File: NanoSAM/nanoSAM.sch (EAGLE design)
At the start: 76 parts, among them IC3 AD5241, J1 POWER_JACK, U1 LTC3260EMSEPBF

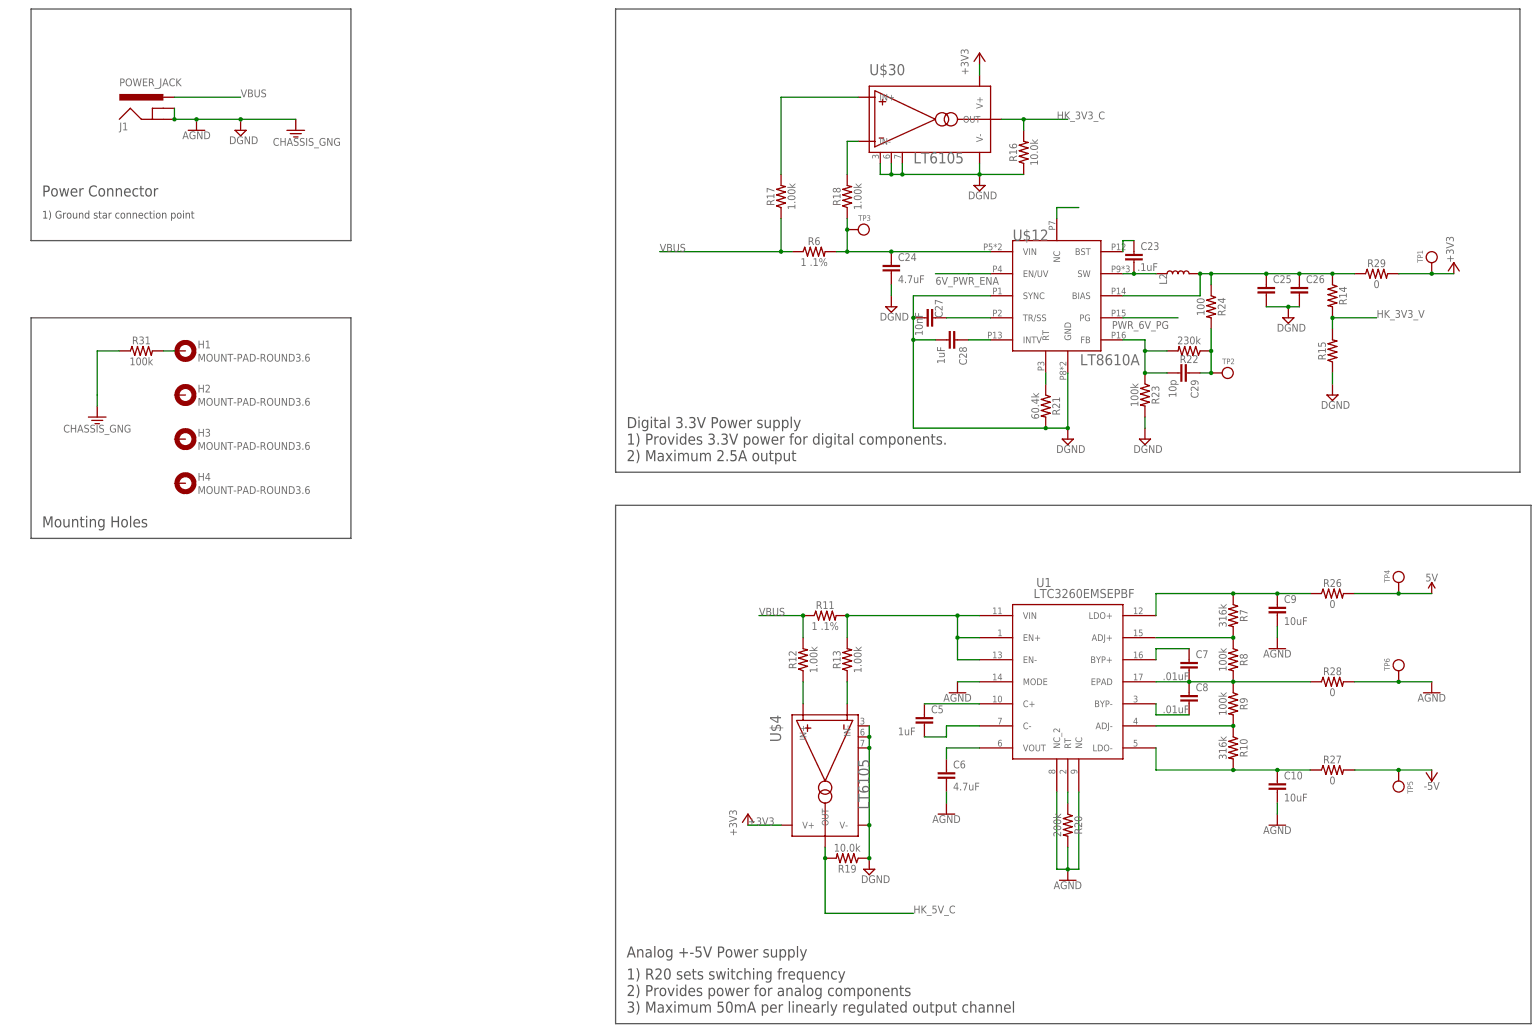
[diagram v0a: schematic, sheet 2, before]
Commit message: added thermistors for temp monitoring and changed current monitoring circuit
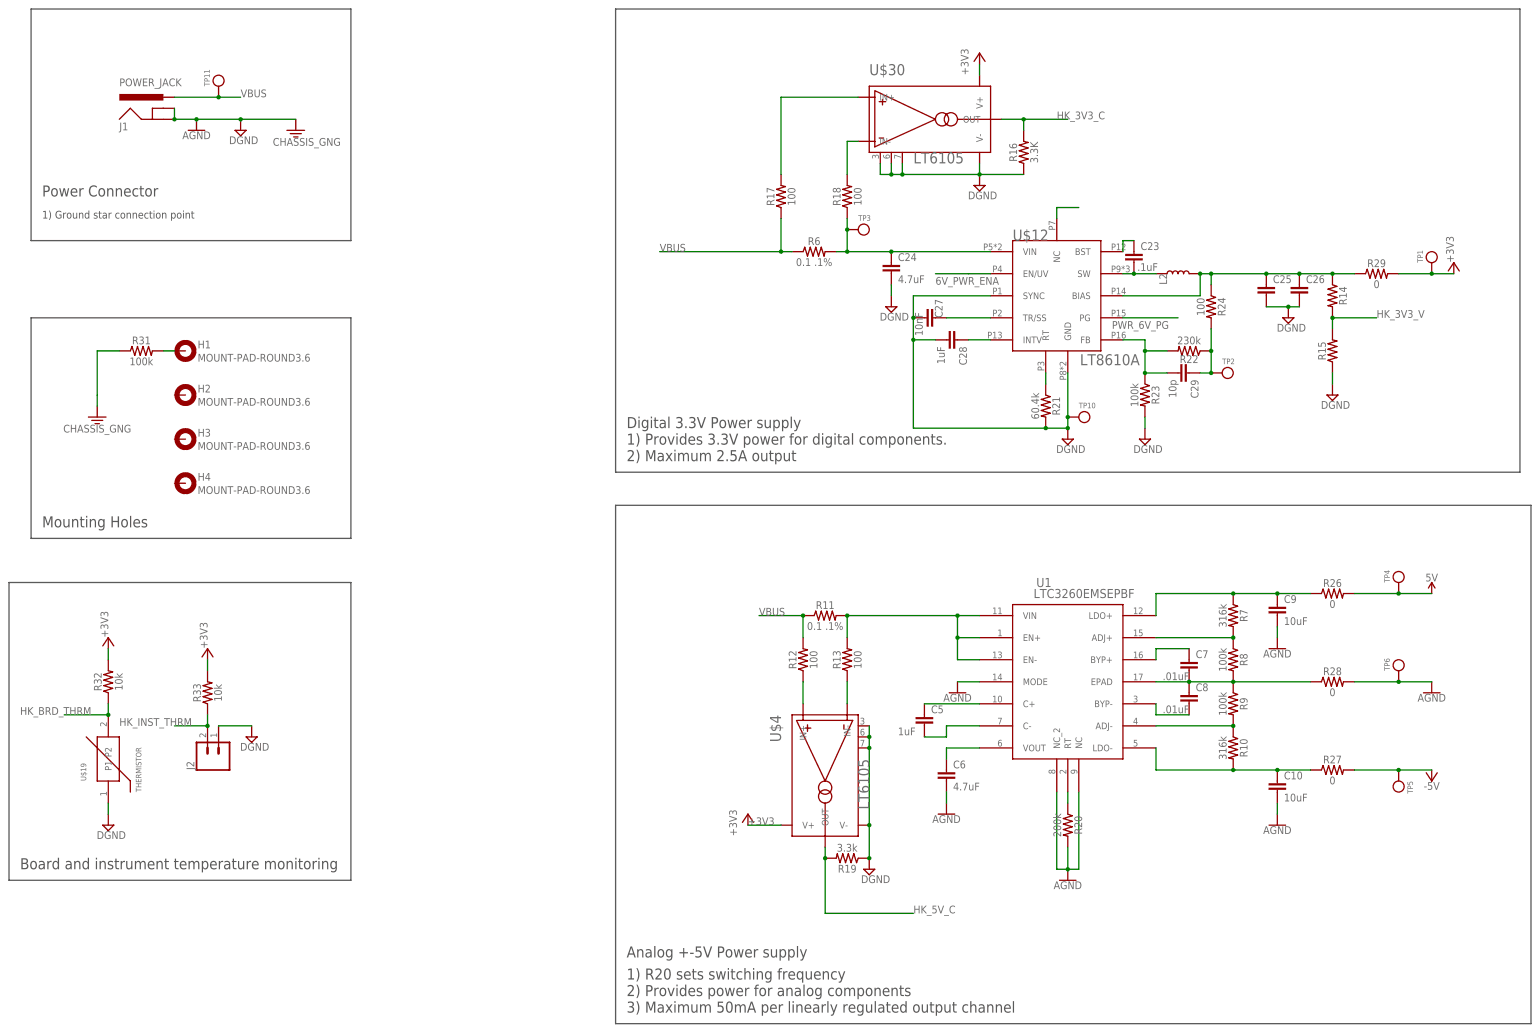
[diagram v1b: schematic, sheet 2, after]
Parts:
- added J2: (no value), SparkFun-Connectors:CONN_02
- added R32, R33: 10k, SparkFun-Resistors:RESISTOR1206
- added TP10, TP11, TP7, TP8, TP9: (no value), testpoint:TESTPOINT
- added U$19: THERMISTOR, 0805_Thermistor:THERMISTOR
- R11, R6: value 1 .1% -> 0.1 .1%
- R12, R13, R17, R18: value 1.00k -> 100
- R16: value 10.0k -> 3.3K
- R19: value 10.0k -> 3.3k
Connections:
- new net HK_BRD_THRM: R32.1, U$19.P2
- new net HK_INST_THRM: J2.2, R33.1
- net +3V3: now also R32.2, R33.2
- net AGND: now also TP9.P$1
- net DGND: now also J2.1, TP10.P$1, U$19.P1
- net N$1: now also TP8.P$1
- net N$3: now also TP7.P$1
- net VBUS: now also TP11.P$1
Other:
- note added: "Board and instrument temperature monitoring"

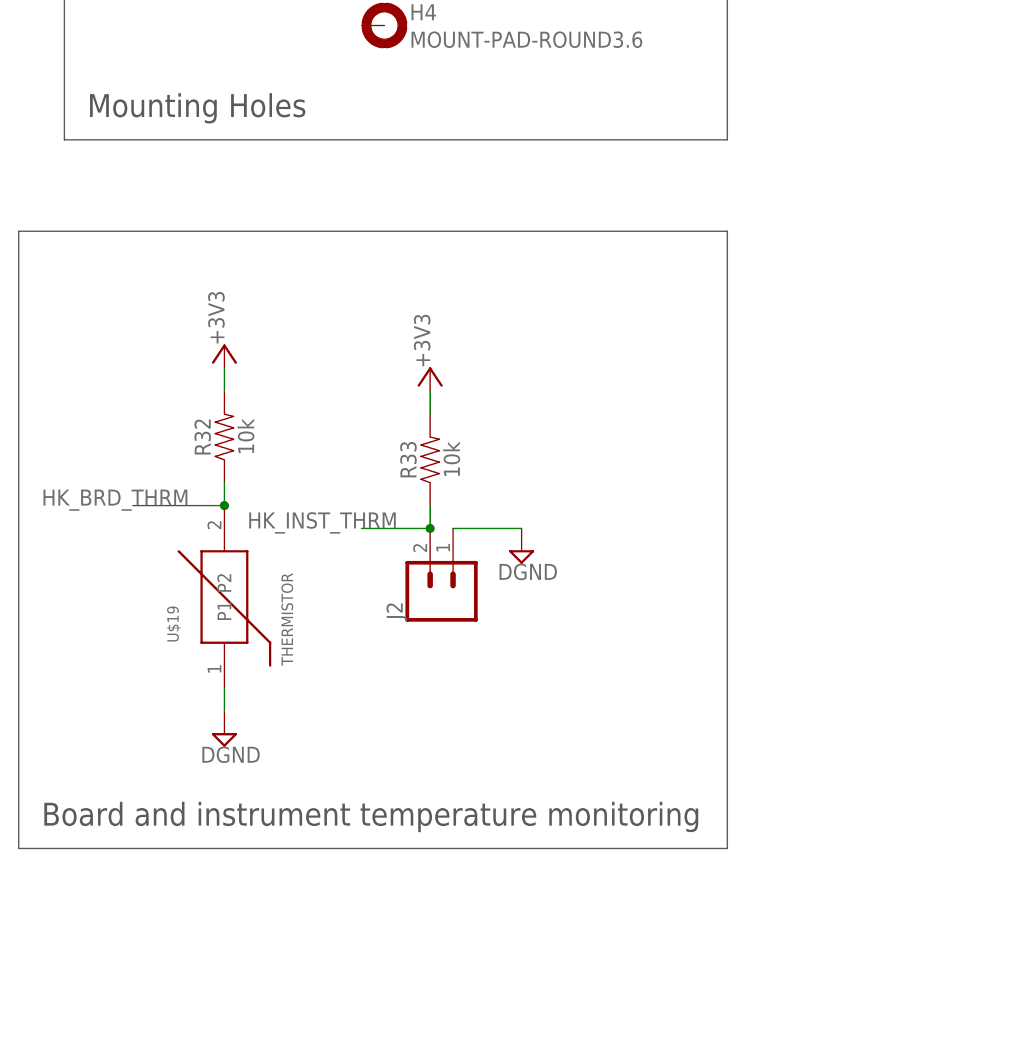
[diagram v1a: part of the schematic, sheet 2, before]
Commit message: added more thermistor connections
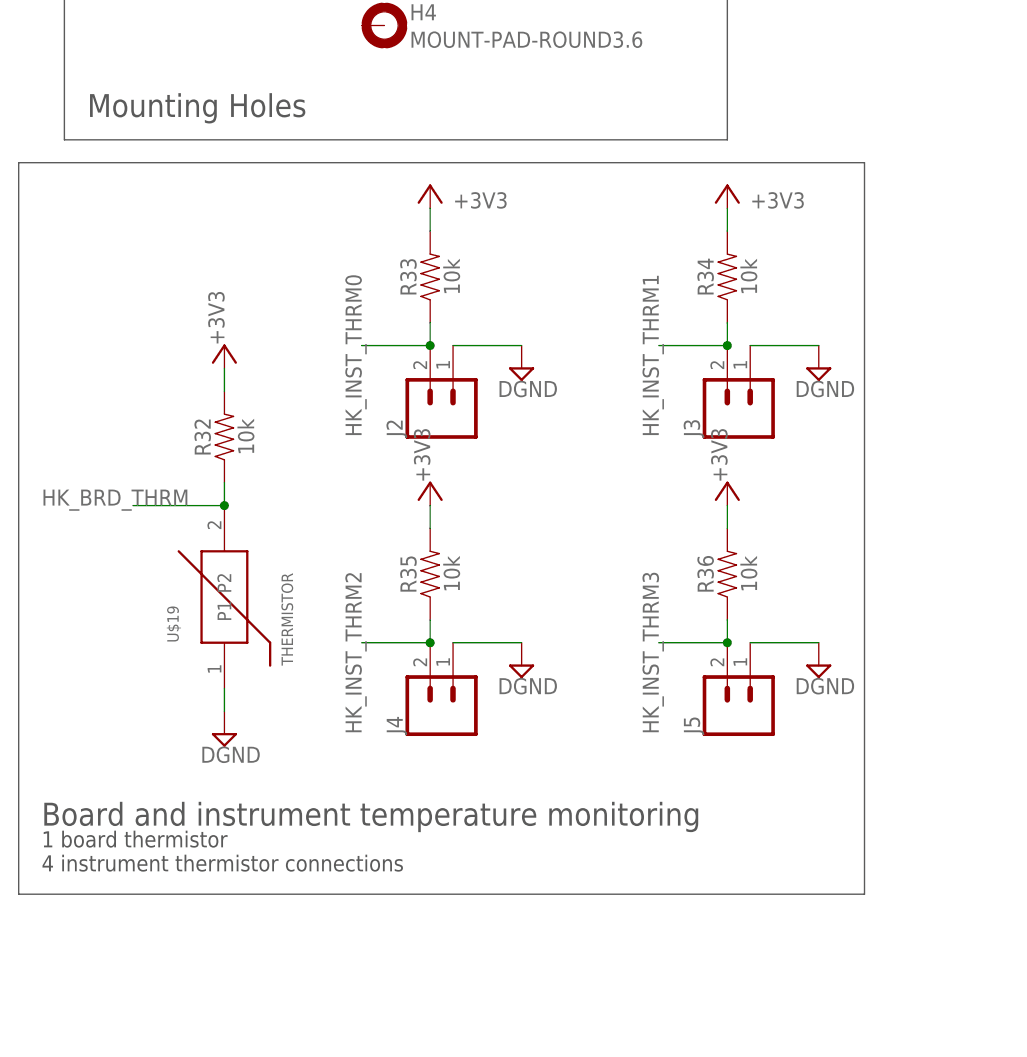
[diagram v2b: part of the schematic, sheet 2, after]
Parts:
- added J3, J4, J5: (no value), SparkFun-Connectors:CONN_02
- added R34, R35, R36: 10k, SparkFun-Resistors:RESISTOR1206
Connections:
- removed net HK_INST_THRM: J2.2, R33.1
- removed net HK_THRM: U$2.D17/A3
- removed net N$25: C4.2, IC3.NC, IC3.VSS
- new net HK_INST_THRM0: J2.2, R33.1, U$2.D20/A6
- new net HK_INST_THRM1: J3.2, R34.1, U$2.D21/A7
- new net HK_INST_THRM2: J4.2, R35.1, U$2.D22/A8
- new net HK_INST_THRM3: J5.2, R36.1, U$2.D23/A9
- net +3V3: now also R34.2, R35.2, R36.2
- net DGND: now also C4.2, IC3.NC, IC3.VSS, J3.1, J4.1, J5.1
- net HK_BRD_THRM: now also U$2.D17/A3
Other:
- note added: "1 board thermistor 4 instrument thermistor connections"
- moved on the sheet: J2, R33

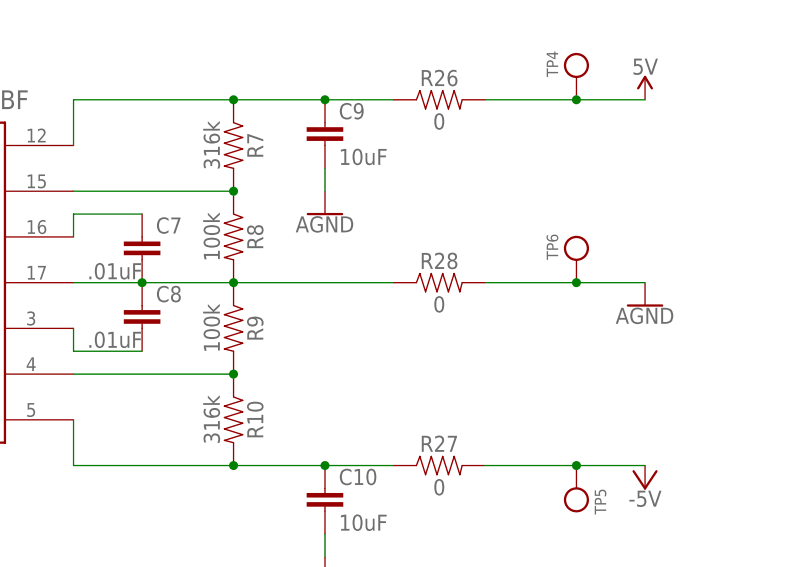
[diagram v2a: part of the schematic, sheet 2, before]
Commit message: Edited Bipolar power supply
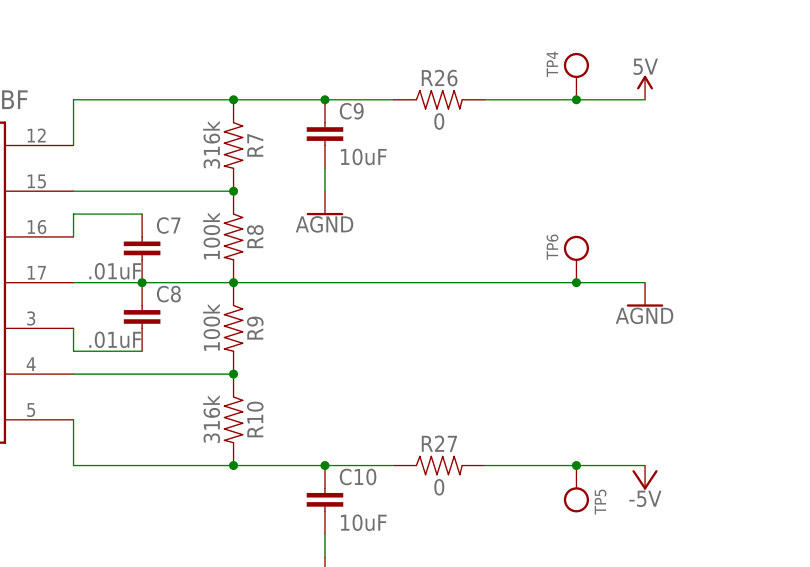
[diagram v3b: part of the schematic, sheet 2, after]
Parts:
- removed R28: 0, SparkFun-Resistors:RESISTOR0603
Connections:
- removed net N$26: C7.2, C8.1, R28.1, R8.2, R9.1, U1.EPAD
- net AGND: now also C7.2, C8.1, R8.2, R9.1, U1.EPAD; no longer R28.2
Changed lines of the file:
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@@
 <?xml version="1.0" encoding="utf-8"?>
 <!DOCTYPE eagle SYSTEM "eagle.dtd">
-<eagle version="9.3.0">
+<eagle version="9.5.1">
 <drawing>
 <settings>
@@
 <part name="R26" library="SparkFun-Resistors" library_urn="urn:adsk.eagle:library:532" deviceset="RESISTOR" device="0603" package3d_urn="urn:adsk.eagle:package:39650/1" value="0"/>
 <part name="R27" library="SparkFun-Resistors" library_urn="urn:adsk.eagle:library:532" deviceset="RESISTOR" device="0603" package3d_urn="urn:adsk.eagle:package:39650/1" value="0"/>
-<part name="R28" library="SparkFun-Resistors" library_urn="urn:adsk.eagle:library:532" deviceset="RESISTOR" device="0603" package3d_urn="urn:adsk.eagle:package:39650/1" value="0"/>
 <part name="TP1" library="testpoint" deviceset="TESTPOINT" device=""/>
 <part name="R29" library="SparkFun-Resistors" library_urn="urn:adsk.eagle:library:532" deviceset="RESISTOR" device="0603" package3d_urn="urn:adsk.eagle:package:39650/1" value="0"/>
@@
 <attribute name="VALUE" x="317.5" y="89.916" size="1.778" layer="96" font="vector" align="top-center"/>
 </instance>
-<instance part="R28" gate="G$1" x="317.5" y="111.76" smashed="yes">
-<attribute name="NAME" x="317.5" y="113.284" size="1.778" layer="95" font="vector" align="bottom-center"/>
-<attribute name="VALUE" x="317.5" y="110.236" size="1.778" layer="96" font="vector" align="top-center"/>
-</instance>
 <instance part="TP1" gate="G$1" x="340.36" y="208.28" smashed="yes" rot="R90">
 <attribute name="NAME" x="338.328" y="208.28" size="1.27" layer="95" rot="R90"/>
@@
 <pinref part="TP6" gate="G$1" pin="P$1"/>
 <junction x="332.74" y="111.76"/>
-<wire x1="322.58" y1="111.76" x2="332.74" y2="111.76" width="0.1524" layer="91"/>
-<pinref part="R28" gate="G$1" pin="2"/>
+<pinref part="R8" gate="G$1" pin="2"/>
+<pinref part="R9" gate="G$1" pin="1"/>
+<wire x1="294.64" y1="111.76" x2="284.48" y2="111.76" width="0.1524" layer="91"/>
+<junction x="294.64" y="111.76"/>
+<pinref part="U1" gate="A" pin="EPAD"/>
+<wire x1="284.48" y1="111.76" x2="276.86" y2="111.76" width="0.1524" layer="91"/>
+<pinref part="C7" gate="G$1" pin="2"/>
+<junction x="284.48" y="111.76"/>
+<pinref part="C8" gate="G$1" pin="1"/>
+<wire x1="294.64" y1="111.76" x2="332.74" y2="111.76" width="0.1524" layer="91"/>
 </segment>
 <segment>
@@
 </segment>
 </net>
-<net name="N$26" class="0">
-<segment>
-<pinref part="R8" gate="G$1" pin="2"/>
-<pinref part="R9" gate="G$1" pin="1"/>
-<wire x1="294.64" y1="111.76" x2="284.48" y2="111.76" width="0.1524" layer="91"/>
-<junction x="294.64" y="111.76"/>
-<pinref part="U1" gate="A" pin="EPAD"/>
-<wire x1="284.48" y1="111.76" x2="276.86" y2="111.76" width="0.1524" layer="91"/>
-<pinref part="C7" gate="G$1" pin="2"/>
-<junction x="284.48" y="111.76"/>
-<pinref part="C8" gate="G$1" pin="1"/>
-<wire x1="294.64" y1="111.76" x2="312.42" y2="111.76" width="0.1524" layer="91"/>
-<pinref part="R28" gate="G$1" pin="1"/>
-</segment>
-</net>
